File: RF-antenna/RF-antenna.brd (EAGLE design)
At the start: 108.2 x 108.2 mm, 9 parts, among them CON1 UMC_CONNECTORREGULAR, X1 LG_HEADER, X2 LG_HEADER, X3 LG_HEADER, X4 SMA-V

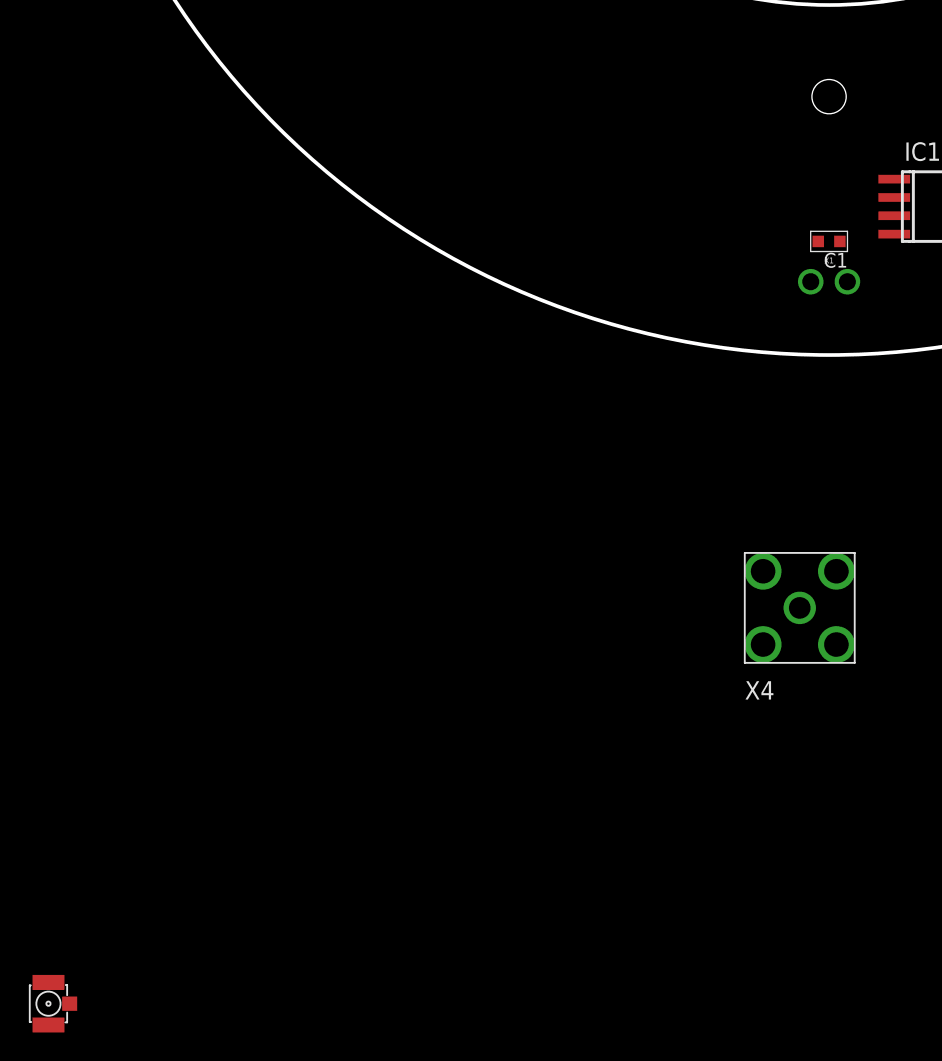
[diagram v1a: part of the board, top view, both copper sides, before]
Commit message: More footprints
Added a few more component footprints to see what is up and test layout.

DSB
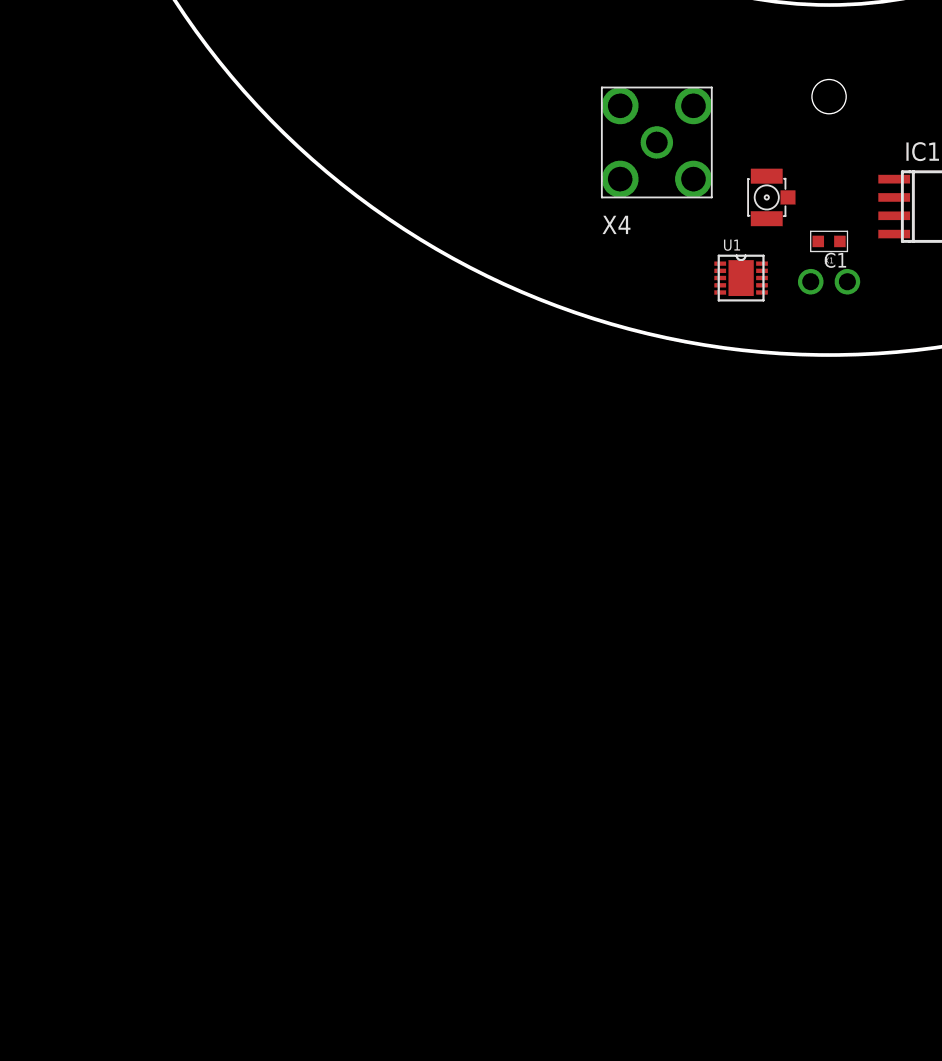
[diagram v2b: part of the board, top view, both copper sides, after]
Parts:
- added U1: (no value), linear-technology-jqi:DFN-10_DD
- moved CON1 74.8 mm to (49.8, 10.9)
- moved X4 33.7 mm to (42.2, 14.7)
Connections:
- new net GND: U1.11
- new net PWRGD: U1.4
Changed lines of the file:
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@@
 <?xml version="1.0" encoding="utf-8"?>
 <!DOCTYPE eagle SYSTEM "eagle.dtd">
-<eagle version="8.5.0">
+<eagle version="7.7.0">
 <drawing>
 <settings>
 <setting alwaysvectorfont="no"/>
-<setting keepoldvectorfont="yes"/>
 <setting verticaltext="up"/>
 </settings>
@@
 <param name="dpMaxLengthDifference" value="10mm"/>
 <param name="dpGapFactor" value="2.5"/>
+<param name="checkGrid" value="0"/>
 <param name="checkAngle" value="0"/>
 <param name="checkFont" value="1"/>
 <param name="checkRestrict" value="1"/>
-<param name="checkStop" value="0"/>
-<param name="checkValues" value="0"/>
 <param name="useDiameter" value="13"/>
 <param name="maxErrors" value="50"/>
@@
 <element name="C2" library="jqi_passives" package="C_MLCC_0603" value="5 pF" x="100.33" y="54.102" rot="R270"/>
 <element name="C3" library="jqi_passives" package="C_MLCC_0603" value="5 pF" x="7.874" y="54.102" rot="R90"/>
-<element name="X4" library="connector-jqi" package="SMA-V" value="SMA-V" x="52.07" y="-17.526"/>
+<element name="X4" library="connector-jqi" package="SMA-V" value="SMA-V" x="42.164" y="14.732"/>
 <element name="IC1" library="opamp-jqi" package="SO08" value="" x="61.214" y="10.922"/>
-<element name="CON1" library="qkdlab_alessandro" package="UMC_CONNECTOR" value="UMC_CONNECTORREGULAR" x="0" y="-44.958"/>
+<element name="CON1" library="qkdlab_alessandro" package="UMC_CONNECTOR" value="UMC_CONNECTORREGULAR" x="49.784" y="10.922"/>
+<element name="U1" library="linear-technology-jqi" package="DFN-10_DD" value="" x="48.006" y="5.334">
+<attribute name="MANUFACTURER_PART_NUMBER" value="lt3065edd#pbf" x="48.006" y="5.334" size="1.778" layer="27" display="off"/>
+<attribute name="VENDOR" value="Linear Technology" x="48.006" y="5.334" size="1.778" layer="27" display="off"/>
+</element>
 </elements>
 <signals>
@@
 <contactref element="IC1" pad="4"/>
 </signal>
+<signal name="PWRGD">
+<contactref element="U1" pad="4"/>
+</signal>
+<signal name="GND">
+<contactref element="U1" pad="11"/>
+</signal>
 </signals>

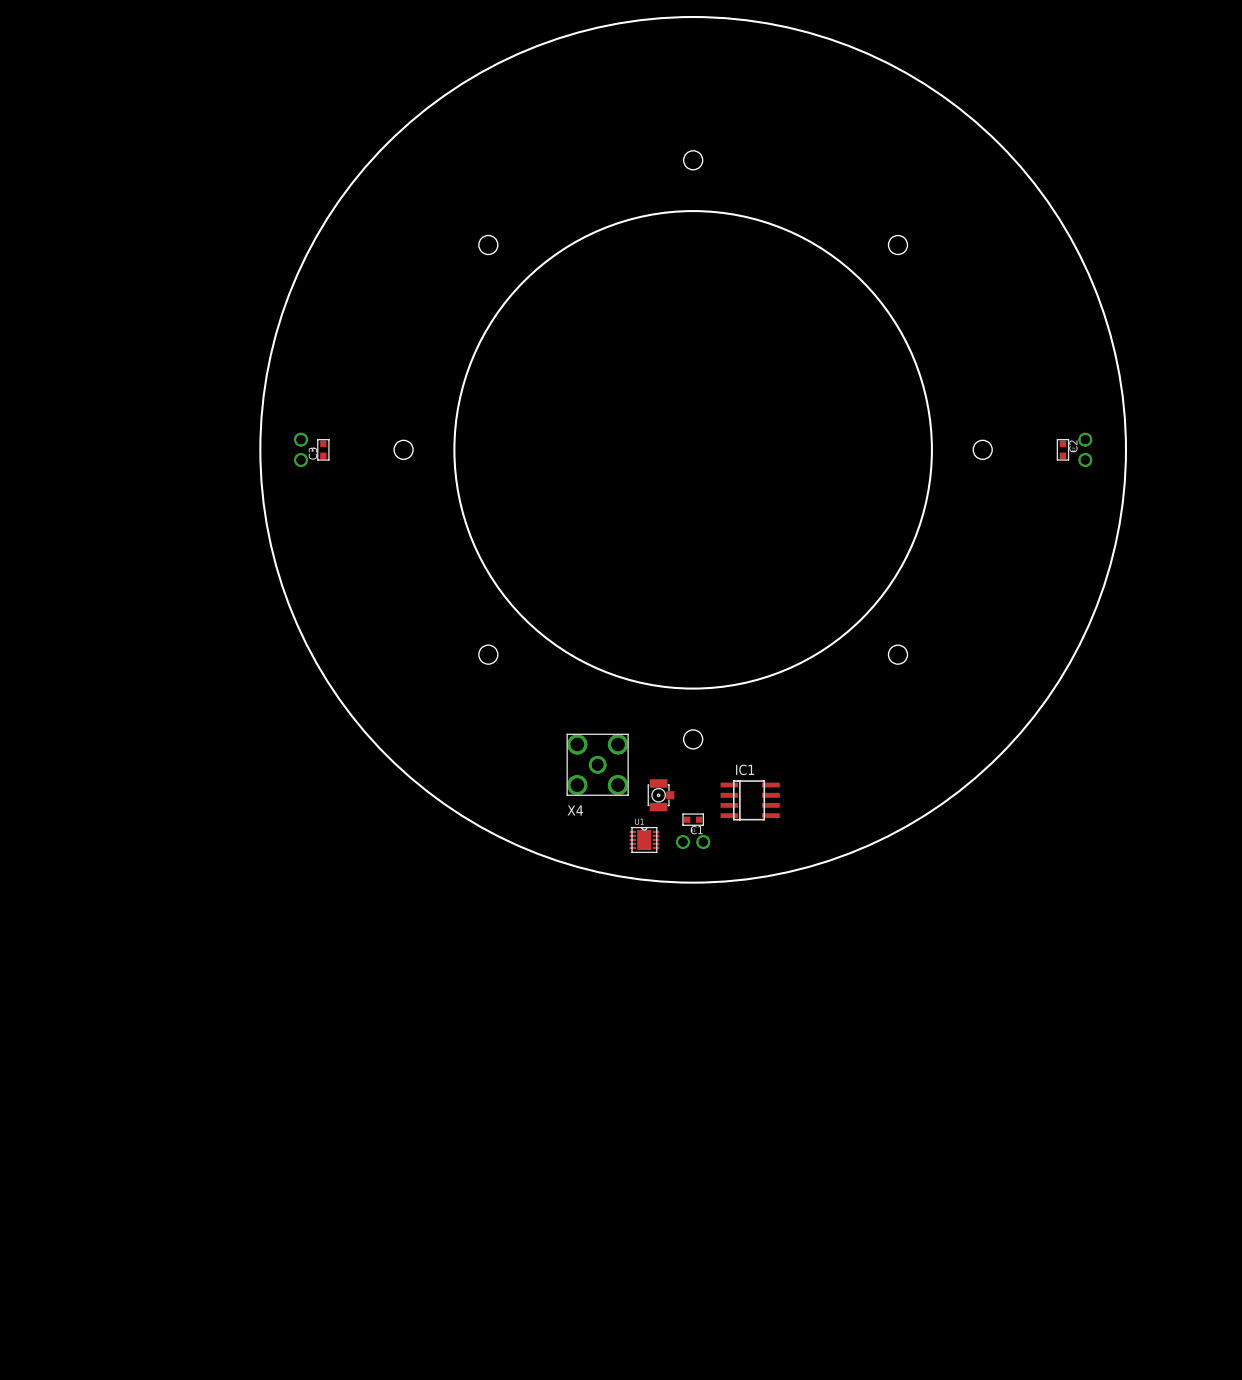
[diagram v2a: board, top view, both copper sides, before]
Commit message: Quick Push
Added buffers and minimal schematic.

DSB
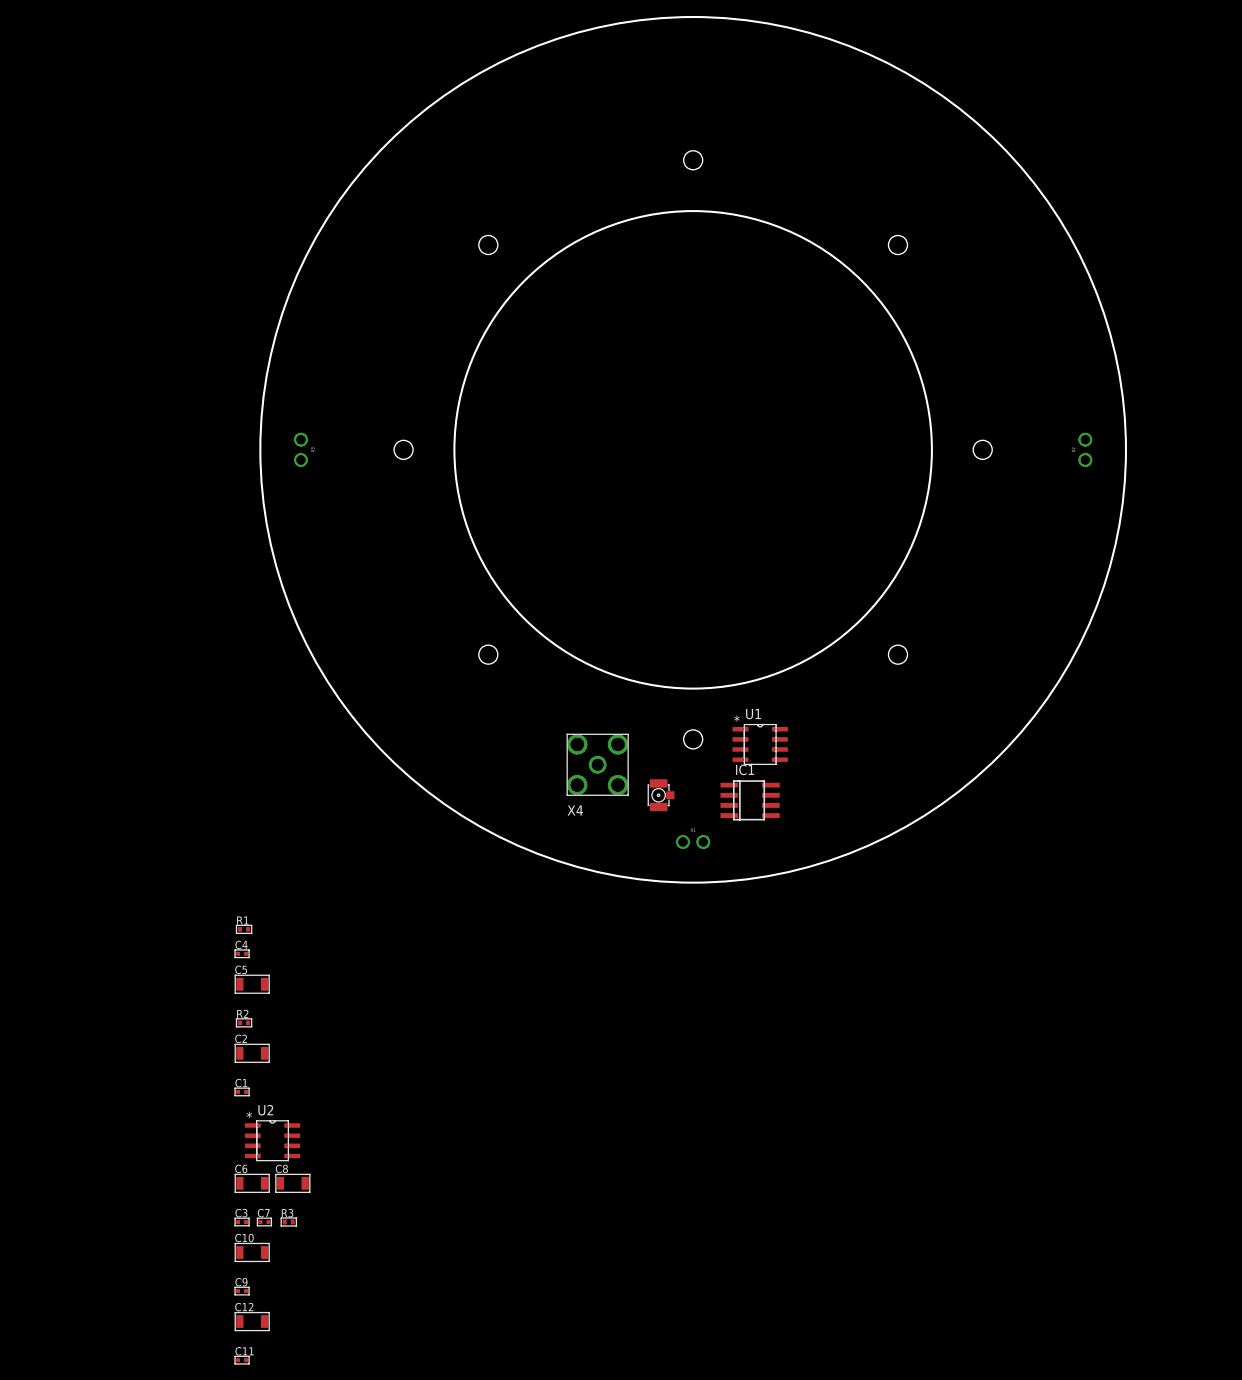
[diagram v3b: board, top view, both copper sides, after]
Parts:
- added C10, C12, C5, C6, C8: 10uF, jqi_passives:C_MLCC_1206
- added C11, C4, C7, C9: 100nF, jqi_passives:C_MLCC_0402
- added R1: 50, jqi_passives:R_0402
- added R2, R3: 10, jqi_passives:R_0402
- added U2: (no value), texas-instruments-jqi:D8
- C1, C3: value 5 pF -> 100nF; device jqi_passives:C_MLCC_0603 -> jqi_passives:C_MLCC_0402
- C2: value 5 pF -> 10uF; device jqi_passives:C_MLCC_0603 -> jqi_passives:C_MLCC_1206
- U1: device linear-technology-jqi:DFN-10_DD -> texas-instruments-jqi:D8
- moved C2 126.3 mm to (-1.02, -21.3), turned to 0 degrees
- moved C3 97.1 mm to (-2.29, -42.4), turned to 0 degrees
- moved C1 65.9 mm to (-2.29, -26.2), turned to 0 degrees
- moved U1 18.8 mm to (62.5, 17.3)
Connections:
- removed net N$2: C2.P$1, C2.P$2, X2.I, X2.R
- removed net N$3: C3.P$1, C3.P$2, X3.I, X3.R
- removed net PWRGD: U1.4
- removed net V+: IC1.7
- new net +15V: C10.P$1, C3.P$1, C4.P$1, C5.P$1, C6.P$1, C9.P$1, IC1.7, U1.7, U2.7
- new net -15V: C1.P$1, C11.P$1, C12.P$1, C2.P$1, C7.P$1, C8.P$1, U1.1, U1.4, U2.1, U2.4
- new net N$4: CON1.P$1, R1.P$2
- new net N$6: R2.P$1, U1.3
- net GND: now also C1.P$2, C10.P$2, C11.P$2, C12.P$2, C2.P$2, C3.P$2, C4.P$2, C5.P$2, C6.P$2, C7.P$2, C8.P$2, C9.P$2, CON1.P$2, CON1.P$3, R1.P$1, U1.2, U1.5, U1.8, U2.2, U2.5, U2.8; no longer U1.11
- net N$1: now also R3.P$1, U2.3; no longer C1.P$1, C1.P$2, X1.I, X1.R

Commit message: Zeroth order design
Quick layout for testing with Alessandro.

DSB
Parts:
- removed C10, C12, C6, C8: 10uF, jqi_passives:C_MLCC_1206
- removed C11, C7, C9: 100nF, jqi_passives:C_MLCC_0402
- removed IC1: (no value), opamp-jqi:SO08
- removed U1, U2: (no value), texas-instruments-jqi:D8
- removed X1, X2, X3: LG_HEADER, connector-jqi:LG_HEADER
- removed X4: SMA-V, connector-jqi:SMA-V
- added CON2: UMC_CONNECTORREGULAR, qkdlab_alessandro:UMC_CONNECTOR
- added JP1: (no value), pinhead:1X03
- added LW1, LW2: LITZ_TERM, RFantenna:LITZ_100MHZ
- added RF: 866, jqi_passives:R_0603
- added U3: THS3091DDAR, opamp-jqi:DDA8_2P28X2P28
- C2: value 10uF -> 100nF; device jqi_passives:C_MLCC_1206 -> jqi_passives:C_MLCC_0402
- C3, C4: value 100nF -> 10uF; device jqi_passives:C_MLCC_0402 -> jqi_passives:C_MLCC_1206
- C5: value 10uF -> 22pF; device jqi_passives:C_MLCC_1206 -> jqi_passives:C_MLCC_0402
- R2: value 10 -> 95.3
- R3: value 10 -> 4.99; device jqi_passives:R_0402 -> jqi_passives:R_1206
- moved C3 80.9 mm to (64.5, 3.30)
- moved C4 69.0 mm to (64.5, 8.38)
- moved C1 68.4 mm to (57.7, 6.86)
- moved R3 67.4 mm to (45.7, 10.2)
- moved C2 64.2 mm to (52.3, 14.5), turned to 180 degrees
- moved R2 59.7 mm to (53.3, 4.83), turned to 270 degrees
- moved R1 59.1 mm to (56.1, 4.83), turned to 90 degrees
- moved C5 58.6 mm to (54.9, 4.83), turned to 90 degrees
- moved CON1 5.23 mm to (47.2, 6.35), turned to 90 degrees
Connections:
- removed net N$6: R2.P$1, U1.3
- removed net V-: IC1.4
- new net N$3: C5.P$2, R1.P$2, U3.3
- new net N$5: CON1.P$1, LW1.T1, LW2.T1, R3.P$2, RF.P$2, U3.6
- net +15V: now also C2.P$1, JP1.3, U3.7; no longer C10.P$1, C3.P$1, C5.P$1, C6.P$1, C9.P$1, IC1.7, U1.7, U2.7
- net -15V: now also C3.P$1, JP1.1, U3.4; no longer C11.P$1, C12.P$1, C2.P$1, C7.P$1, C8.P$1, U1.1, U1.4, U2.1, U2.4
- net GND: now also CON2.P$2, CON2.P$3, JP1.2, R2.P$2, R3.P$1, U3.1, U3.5, U3.8, U3.EPAD, U3.P$1, U3.P$10, U3.P$11, U3.P$12, U3.P$13, U3.P$2, U3.P$3, U3.P$4, U3.P$5, U3.P$6, U3.P$7, U3.P$8, U3.P$9; no longer C10.P$2, C11.P$2, C12.P$2, C5.P$2, C6.P$2, C7.P$2, C8.P$2, C9.P$2, U1.2, U1.5, U1.8, U2.2, U2.5, U2.8
- net N$1: now also R2.P$1, RF.P$1, U3.2; no longer R3.P$1, U2.3
- net N$4: now also C5.P$1, CON2.P$1; no longer CON1.P$1, R1.P$2
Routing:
- net N$5: track 0.00 -> 39.9 mm
- net +15V: track 0.00 -> 16.2 mm, vias 0 -> 1
- net -15V: track 0.00 -> 9.73 mm
- net N$1: track 0.00 -> 7.21 mm
- net N$3: track 0.00 -> 3.12 mm
- net N$4: track 0.00 -> 1.07 mm
- added copper zone on layer 1, net GND
- added copper zone on layer 16, net GND
